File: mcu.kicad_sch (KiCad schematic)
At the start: 6 parts, among them U10 PIC18F24K42

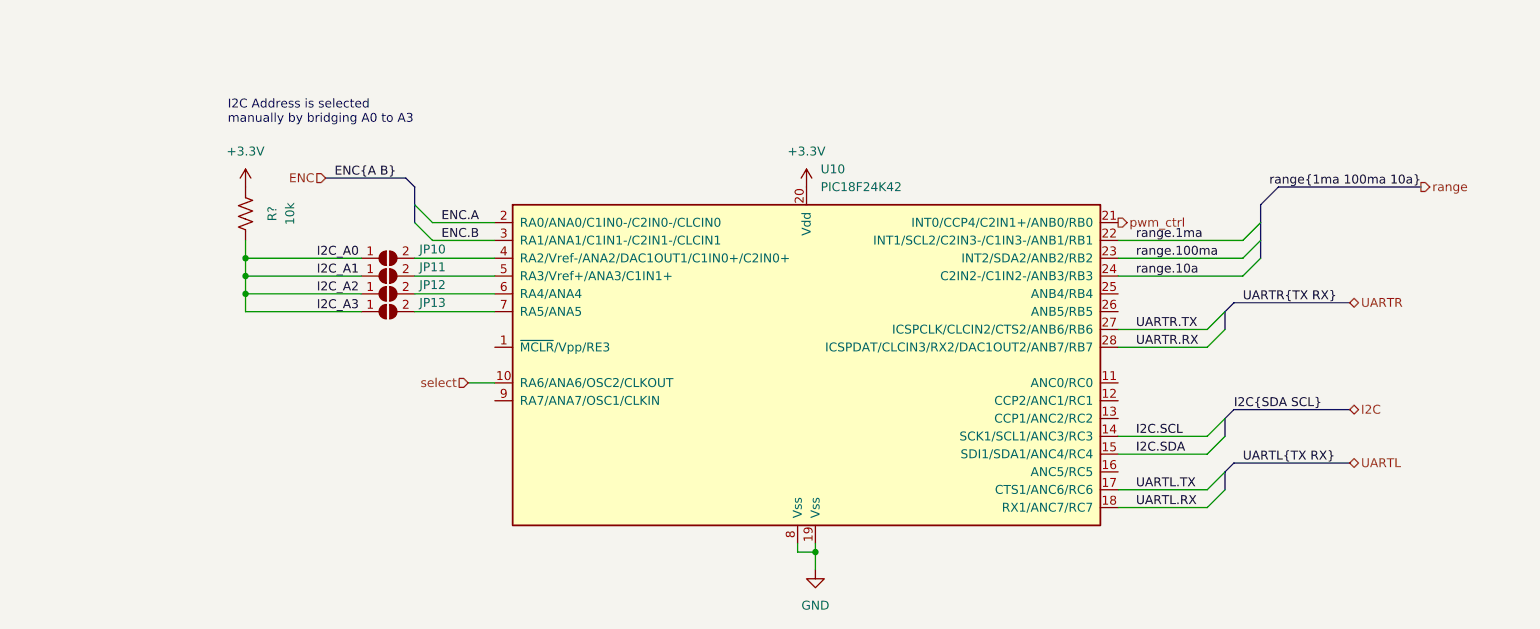
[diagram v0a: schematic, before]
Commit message: Replace UART{R,L} with I2C
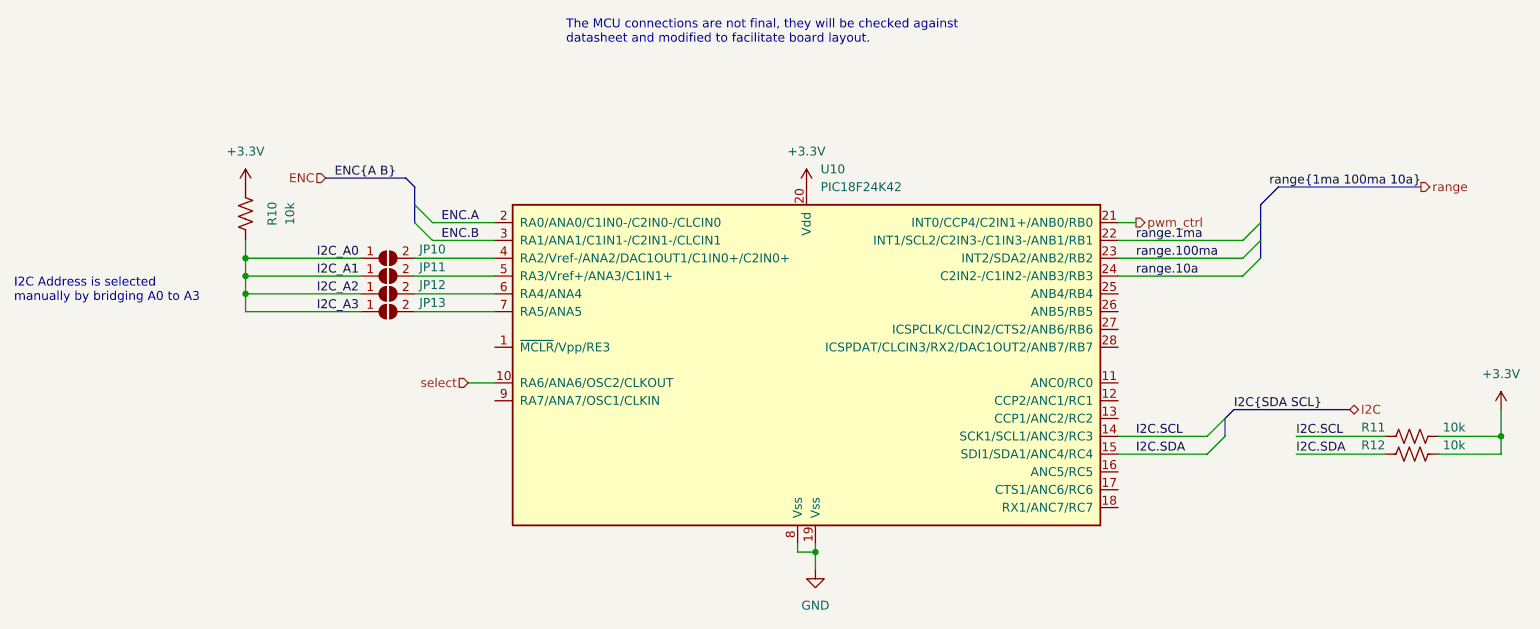
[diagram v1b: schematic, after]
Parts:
- added R11, R12: 10k, Resistor_SMD:R_0805_2012Metric, symbol Device:R_US
- gave numbers to parts that had none: 1
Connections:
- net +3V3: now also R11.1, R12.1
- net I2C.SCL: now also R11.2
- net I2C.SDA: now also R12.2
- net UARTL.RX: no longer names the net of U10.18 (RX1/ANC7/RC7)
- net UARTL.TX: no longer names the net of U10.17 (CTS1/ANC6/RC6)
- net UARTR.RX: no longer names the net of U10.28 (ICSPDAT/CLCIN3/RX2/DAC1OUT2/ANB7/RB7)
- net UARTR.TX: no longer names the net of U10.27 (ICSPCLK/CLCIN2/CTS2/ANB6/RB6)
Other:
- note added: "The MCU connections are not final, they will be checked against datasheet and modified to facilitate board layout."
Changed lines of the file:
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@@
 (kicad_sch (version 20211123) (generator eeschema)
   (paper "A4")
+  (junction (at 241.3 113.03) (diameter 0) (color 0 0 0 0)
+  )
   (junction (at 143.51 129.54) (diameter 0) (color 0 0 0 0)
   )
@@
     (stroke (width 0) (type default) (color 0 0 0 0))
   )
-  (bus_entry (at 201.93 120.65) (size -2.54 2.54)
-    (stroke (width 0) (type default) (color 0 0 0 0))
-  )
-  (bus_entry (at 201.93 95.25) (size -2.54 2.54)
-    (stroke (width 0) (type default) (color 0 0 0 0))
-  )
-  (bus_entry (at 201.93 97.79) (size -2.54 2.54)
-    (stroke (width 0) (type default) (color 0 0 0 0))
-  )
   (bus_entry (at 201.93 113.03) (size -2.54 2.54)
     (stroke (width 0) (type default) (color 0 0 0 0))
@@
     (stroke (width 0) (type default) (color 0 0 0 0))
   )
-  (bus_entry (at 201.93 118.11) (size -2.54 2.54)
-    (stroke (width 0) (type default) (color 0 0 0 0))
-  )
   (bus_entry (at 207.01 85.09) (size -2.54 2.54)
     (stroke (width 0) (type default) (color 0 0 0 0))
@@
     (stroke (width 0) (type default) (color 0 0 0 0))
   )
-  (bus (pts (xy 201.93 118.11) (xy 201.93 120.65))
-    (stroke (width 0) (type default) (color 0 0 0 0))
-  )
-  (bus (pts (xy 201.93 95.25) (xy 201.93 97.79))
-    (stroke (width 0) (type default) (color 0 0 0 0))
-  )
   (wire (pts (xy 62.23 90.17) (xy 78.74 90.17))
     (stroke (width 0) (type default) (color 0 0 0 0))
@@
     (stroke (width 0) (type default) (color 0 0 0 0))
   )
-  (wire (pts (xy 186.69 120.65) (xy 199.39 120.65))
-    (stroke (width 0) (type default) (color 0 0 0 0))
-  )
   (wire (pts (xy 88.9 82.55) (xy 97.79 82.55))
     (stroke (width 0) (type default) (color 0 0 0 0))
   )
+  (wire (pts (xy 241.3 113.03) (xy 241.3 109.22))
+    (stroke (width 0) (type default) (color 0 0 0 0))
+  )
+  (wire (pts (xy 241.3 115.57) (xy 241.3 113.03))
+    (stroke (width 0) (type default) (color 0 0 0 0))
+  )
   (wire (pts (xy 62.23 87.63) (xy 62.23 85.09))
     (stroke (width 0) (type default) (color 0 0 0 0))
@@
     (stroke (width 0) (type default) (color 0 0 0 0))
   )
+  (wire (pts (xy 232.41 115.57) (xy 241.3 115.57))
+    (stroke (width 0) (type default) (color 0 0 0 0))
+  )
   (wire (pts (xy 62.23 95.25) (xy 62.23 92.71))
     (stroke (width 0) (type default) (color 0 0 0 0))
@@
     (stroke (width 0) (type default) (color 0 0 0 0))
   )
-  (wire (pts (xy 186.69 123.19) (xy 199.39 123.19))
-    (stroke (width 0) (type default) (color 0 0 0 0))
-  )
-  (wire (pts (xy 186.69 100.33) (xy 199.39 100.33))
-    (stroke (width 0) (type default) (color 0 0 0 0))
-  )
   (wire (pts (xy 88.9 85.09) (xy 97.79 85.09))
     (stroke (width 0) (type default) (color 0 0 0 0))
@@
     (stroke (width 0) (type default) (color 0 0 0 0))
   )
-  (bus (pts (xy 219.71 116.84) (xy 203.2 116.84))
-    (stroke (width 0) (type default) (color 0 0 0 0))
-  )
   (bus (pts (xy 86.36 80.01) (xy 86.36 82.55))
     (stroke (width 0) (type default) (color 0 0 0 0))
@@
     (stroke (width 0) (type default) (color 0 0 0 0))
   )
+  (wire (pts (xy 189.23 82.55) (xy 186.69 82.55))
+    (stroke (width 0) (type default) (color 0 0 0 0))
+  )
   (wire (pts (xy 140.97 129.54) (xy 143.51 129.54))
     (stroke (width 0) (type default) (color 0 0 0 0))
   )
+  (wire (pts (xy 212.09 115.57) (xy 224.79 115.57))
+    (stroke (width 0) (type default) (color 0 0 0 0))
+  )
   (wire (pts (xy 186.69 115.57) (xy 199.39 115.57))
     (stroke (width 0) (type default) (color 0 0 0 0))
@@
     (stroke (width 0) (type default) (color 0 0 0 0))
   )
-  (bus (pts (xy 203.2 116.84) (xy 201.93 118.11))
-    (stroke (width 0) (type default) (color 0 0 0 0))
-  )
-  (wire (pts (xy 186.69 97.79) (xy 199.39 97.79))
-    (stroke (width 0) (type default) (color 0 0 0 0))
-  )
-  (bus (pts (xy 203.2 93.98) (xy 201.93 95.25))
+  (wire (pts (xy 232.41 113.03) (xy 241.3 113.03))
+    (stroke (width 0) (type default) (color 0 0 0 0))
+  )
+  (wire (pts (xy 212.09 113.03) (xy 224.79 113.03))
     (stroke (width 0) (type default) (color 0 0 0 0))
   )
@@
     (stroke (width 0) (type default) (color 0 0 0 0))
   )
-  (bus (pts (xy 219.71 93.98) (xy 203.2 93.98))
-    (stroke (width 0) (type default) (color 0 0 0 0))
-  )
   (bus (pts (xy 207.01 82.55) (xy 207.01 85.09))
     (stroke (width 0) (type default) (color 0 0 0 0))
   )
   (text "I2C Address is selected \nmanually by bridging A0 to A3"
-    (at 59.69 68.58 0)
-    (effects (font (size 1.27 1.27)) (justify left bottom))
-  )
-  (label "UARTL.RX" (at 189.23 123.19 0)
+    (at 29.21 93.98 0)
+    (effects (font (size 1.27 1.27)) (justify left bottom))
+  )
+  (text "The MCU connections are not final, they will be checked against \ndatasheet and modified to facilitate board layout."
+    (at 107.95 57.15 0)
     (effects (font (size 1.27 1.27)) (justify left bottom))
   )
@@
     (effects (font (size 1.27 1.27)) (justify left bottom))
   )
-  (label "UARTL{TX RX}" (at 204.47 116.84 0)
-    (effects (font (size 1.27 1.27)) (justify left bottom))
-  )
   (label "I2C_A0" (at 72.39 87.63 0)
     (effects (font (size 1.27 1.27)) (justify left bottom))
@@
     (effects (font (size 1.27 1.27)) (justify left bottom))
   )
-  (label "UARTL.TX" (at 189.23 120.65 0)
+  (label "I2C.SDA" (at 212.09 115.57 0)
+    (effects (font (size 1.27 1.27)) (justify left bottom))
+  )
+  (label "I2C.SCL" (at 212.09 113.03 0)
     (effects (font (size 1.27 1.27)) (justify left bottom))
   )
   (label "I2C_A1" (at 72.39 90.17 0)
-    (effects (font (size 1.27 1.27)) (justify left bottom))
-  )
-  (label "UARTR.RX" (at 189.23 100.33 0)
     (effects (font (size 1.27 1.27)) (justify left bottom))
   )
@@
     (effects (font (size 1.27 1.27)) (justify right bottom))
   )
-  (label "UARTR{TX RX}" (at 204.47 93.98 0)
-    (effects (font (size 1.27 1.27)) (justify left bottom))
-  )
   (label "ENC.A" (at 90.17 82.55 0)
     (effects (font (size 1.27 1.27)) (justify left bottom))
   )
-  (label "UARTR.TX" (at 189.23 97.79 0)
-    (effects (font (size 1.27 1.27)) (justify left bottom))
-  )
   (label "I2C.SCL" (at 189.23 113.03 0)
     (effects (font (size 1.27 1.27)) (justify left bottom))
@@
     (effects (font (size 1.27 1.27)) (justify left bottom))
   )
-  (hierarchical_label "pwm_ctrl" (shape output) (at 186.69 82.55 0)
+  (hierarchical_label "pwm_ctrl" (shape output) (at 189.23 82.55 0)
     (effects (font (size 1.27 1.27)) (justify left))
   )
@@
     (effects (font (size 1.27 1.27)) (justify left))
   )
-  (hierarchical_label "UARTR" (shape bidirectional) (at 219.71 93.98 0)
-    (effects (font (size 1.27 1.27)) (justify left))
-  )
   (hierarchical_label "ENC" (shape input) (at 73.66 76.2 180)
     (effects (font (size 1.27 1.27)) (justify right))
   )
-  (hierarchical_label "UARTL" (shape bidirectional) (at 219.71 116.84 0)
-    (effects (font (size 1.27 1.27)) (justify left))
-  )
   (hierarchical_label "range" (shape output) (at 229.87 77.47 0)
     (effects (font (size 1.27 1.27)) (justify left))
+  )
+  (symbol (lib_id "Device:R_US") (at 228.6 115.57 270) (unit 1)
+    (in_bom yes) (on_board yes)
+    (property "Reference" "R12" (id 0) (at 224.79 114.3 90)
+      (effects (font (size 1.27 1.27)) (justify right))
+    )
+    (property "Value" "10k" (id 1) (at 236.22 114.3 90)
+      (effects (font (size 1.27 1.27)) (justify right))
+    )
+    (property "Footprint" "Resistor_SMD:R_0805_2012Metric" (id 2) (at 228.346 116.586 90)
+      (effects (font (size 1.27 1.27)) hide)
+    )
+    (property "Datasheet" "~" (id 3) (at 228.6 115.57 0)
+      (effects (font (size 1.27 1.27)) hide)
+    )
+    (pin "1")
+    (pin "2")
   )
   (symbol (lib_id "Jumper:SolderJumper_2_Open") (at 82.55 87.63 0) (unit 1)
@@
     (pin "1")
   )
+  (symbol (lib_id "power:+3.3V") (at 241.3 109.22 0) (unit 1)
+    (in_bom yes) (on_board yes)
+    (property "Reference" "#PWR?" (id 0) (at 241.3 113.03 0)
+      (effects (font (size 1.27 1.27)) hide)
+    )
+    (property "Value" "+3.3V" (id 1) (at 241.3 104.14 0))
+    (property "Footprint" "" (id 2) (at 241.3 109.22 0)
+      (effects (font (size 1.27 1.27)) hide)
+    )
+    (property "Datasheet" "" (id 3) (at 241.3 109.22 0)
+      (effects (font (size 1.27 1.27)) hide)
+    )
+    (pin "1")
+  )
   (symbol (lib_id "Device:R_US") (at 62.23 81.28 180) (unit 1)
     (in_bom yes) (on_board yes)
-    (property "Reference" "R?" (id 0) (at 66.04 81.28 90))
+    (property "Reference" "R10" (id 0) (at 66.04 81.28 90))
     (property "Value" "10k" (id 1) (at 68.58 81.28 90))
     (property "Footprint" "Resistor_SMD:R_0805_2012Metric" (id 2) (at 61.214 81.026 90)
@@
     (pin "2")
   )
+  (symbol (lib_id "Device:R_US") (at 228.6 113.03 270) (unit 1)
+    (in_bom yes) (on_board yes)
+    (property "Reference" "R11" (id 0) (at 224.79 111.76 90)
+      (effects (font (size 1.27 1.27)) (justify right))
+    )
+    (property "Value" "10k" (id 1) (at 236.22 111.76 90)
+      (effects (font (size 1.27 1.27)) (justify right))
+    )
+    (property "Footprint" "Resistor_SMD:R_0805_2012Metric" (id 2) (at 228.346 114.046 90)
+      (effects (font (size 1.27 1.27)) hide)
+    )
+    (property "Datasheet" "~" (id 3) (at 228.6 113.03 0)
+      (effects (font (size 1.27 1.27)) hide)
+    )
+    (pin "1")
+    (pin "2")
+  )
   (symbol (lib_id "Jumper:SolderJumper_2_Open") (at 82.55 92.71 0) (unit 1)
     (in_bom yes) (on_board yes)
@@
   )
   (symbol (lib_id "power:+3.3V") (at 142.24 77.47 0) (unit 1)
-    (in_bom yes) (on_board yes) (fields_autoplaced)
+    (in_bom yes) (on_board yes)
     (property "Reference" "#PWR0108" (id 0) (at 142.24 81.28 0)
       (effects (font (size 1.27 1.27)) hide)

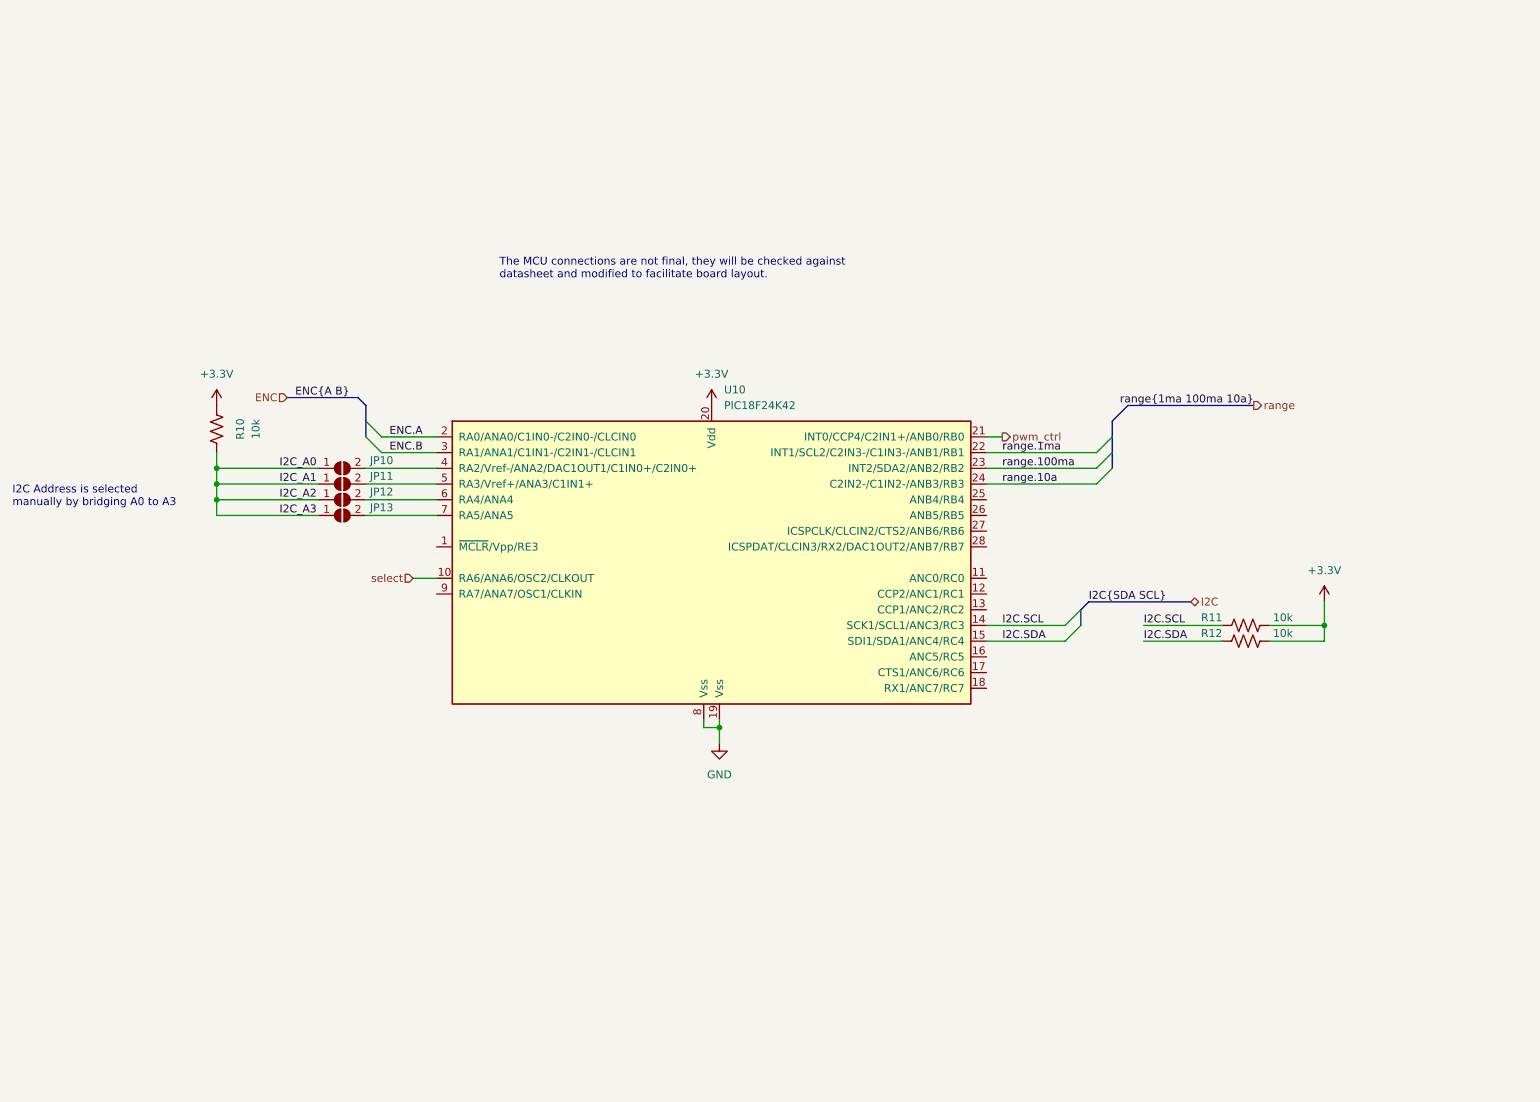
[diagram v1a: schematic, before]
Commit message: Add voltage reference and voltage regulator
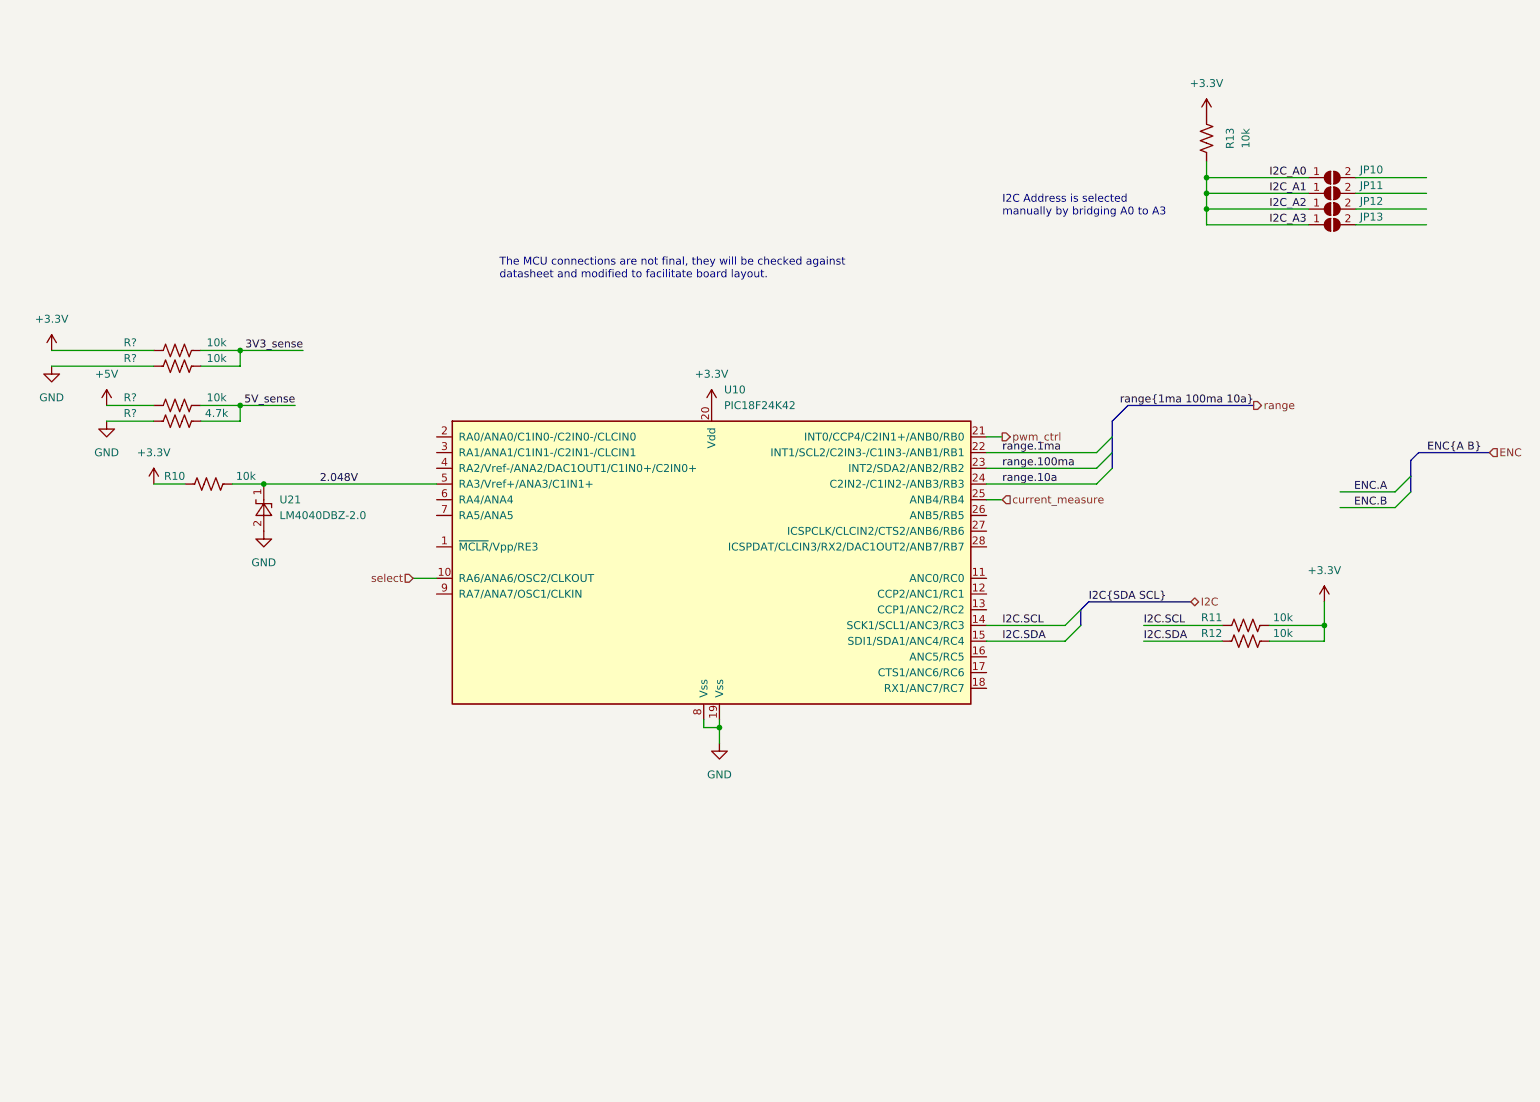
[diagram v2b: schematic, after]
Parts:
- added R10, R? (x3): 10k, Resistor_SMD:R_0805_2012Metric, symbol Device:R_US
- added R?: 4.7k, Resistor_SMD:R_0805_2012Metric, symbol Device:R_US
- added U21: LM4040DBZ-2.0, Package_TO_SOT_SMD:SOT-23, symbol Reference_Voltage:LM4040DBZ-2.0
- renumbered R10 to R13
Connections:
- net +3V3: now also R10.2, R?.2
- net ENC.A: no longer U10.2 (RA0/ANA0/C1IN0-/C2IN0-/CLCIN0)
- net ENC.B: no longer U10.3 (RA1/ANA1/C1IN1-/C2IN1-/CLCIN1)
- net GND: now also R?.1, R?.1, U21.2 (A)
- net at JP10.2 (B): no longer U10.4 (RA2/Vref-/ANA2/DAC1OUT1/C1IN0+/C2IN0+)
- net current_measure: now reaches U10.25 (ANB4/RB4)
- net at JP11.2 (B): no longer U10.5 (RA3/Vref+/ANA3/C1IN1+)
- net at U10.6 (RA4/ANA4): no longer JP12.2 (B)
- net at U10.7 (RA5/ANA5): no longer JP13.2 (B)
- new net +5V: R?.2
- new net 2.048V: R10.1, U10.5 (RA3/Vref+/ANA3/C1IN1+), U21.1 (K)
- new net 3V3_sense: R?.1, R?.2
- new net 5V_sense: R?.1, R?.2
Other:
- moved on the sheet: JP10, JP11, JP12, JP13, R13
